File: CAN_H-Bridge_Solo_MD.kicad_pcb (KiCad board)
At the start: 2 copper layers, 84.9 x 45.3 mm, 45 parts, among them IC1 SI8650AB-B-IS1, IC2 A3921KLPTR-T, J2 Conn_01x03, J3 Conn_01x05, J4 Bus_mechaken_PCIexpress_x16_1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, M1 Motor_DC, Q1 IRLB3813PBF, Q2 IRLB3813PBF, Q3 IRLB3813PBF, Q4 IRLB3813PBF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

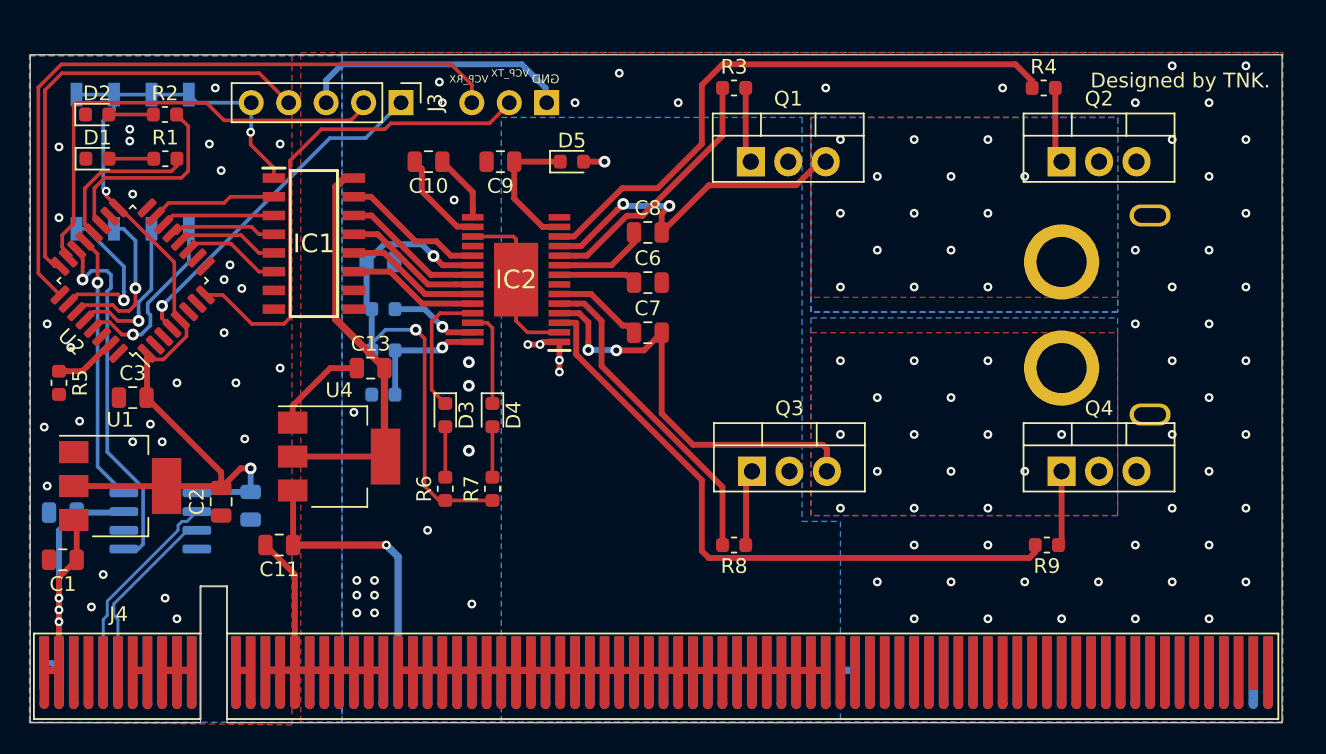
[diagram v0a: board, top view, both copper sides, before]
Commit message: change
FETのドレイン端子を移動
パッドを手はんだ用に変更
PCIeコネクタを変更
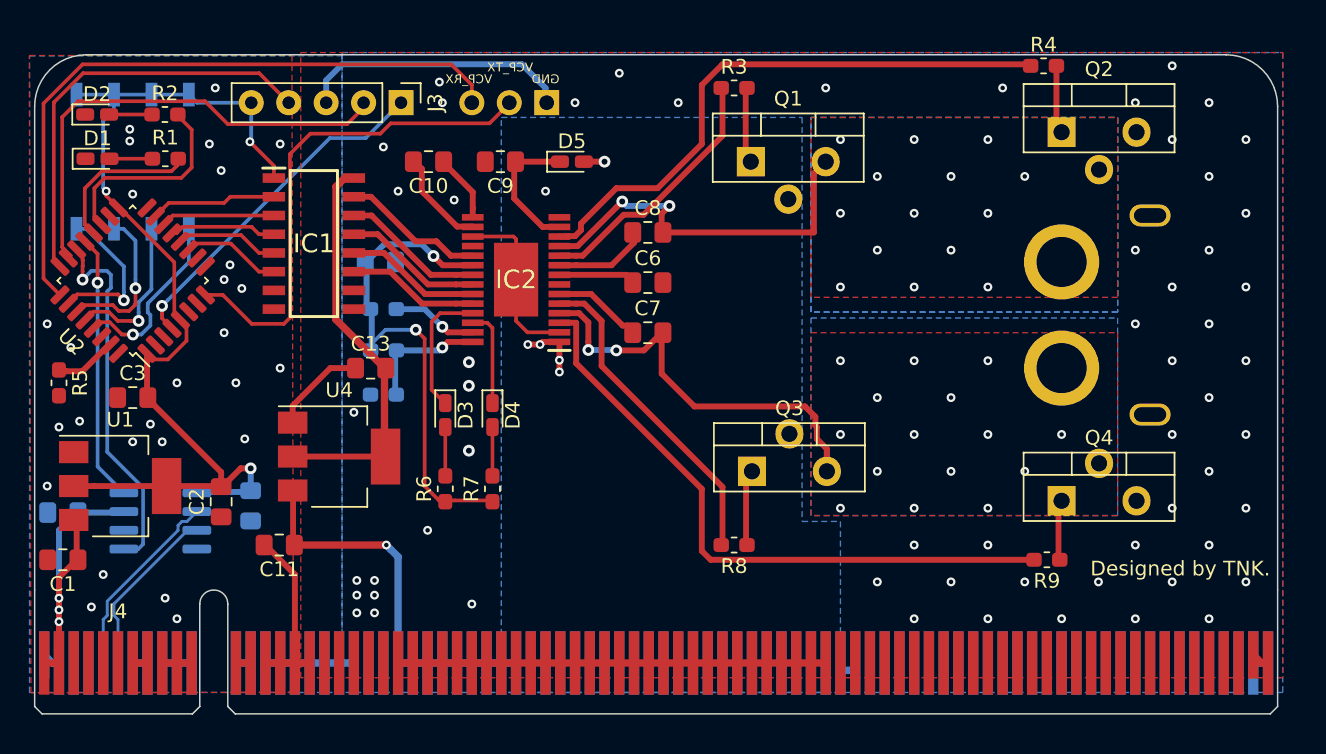
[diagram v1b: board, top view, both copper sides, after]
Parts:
- C1, C10, C11, C12, C13, C2, C3, C4, C5, C6, C7, C8, C9: footprint Capacitor_SMD:C_0805_2012Metric -> Capacitor_SMD:C_0805_2012Metric_Pad1.15x1.40mm_HandSolder
- D1, D2, D3, D4: footprint LED_SMD:LED_0603_1608Metric -> LED_SMD:LED_0603_1608Metric_Castellated
- D5: footprint Diode_SMD:D_0603_1608Metric -> LED_SMD:LED_0603_1608Metric_Castellated
- J4: footprint PCIe:BUS_mechaken_PCIexpress_x16_164_Position -> PCIe:BUS_mechaken_PCIexpress_x16
- R1, R10, R11, R12, R2, R3, R4, R5, R6, R7, R8, R9: footprint Resistor_SMD:R_0603_1608Metric -> Resistor_SMD:R_0603_1608Metric_Pad1.05x0.95mm_HandSolder
- moved Q2 2.00 mm to (145.0, 122.0)
- moved Q4 2.00 mm to (145.0, 147.0)
- moved R4 1.50 mm to (143.8, 117.5)
- moved R9 1.00 mm to (144.0, 151.0)
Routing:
- net GNDPWR: track 44.7 -> 39.9 mm, vias 57 -> 59
- net SA_0: track 23.8 -> 26.3 mm
- net /SWCLK: track 30.4 -> 28.9 mm
- net VCP_RX: track 46.5 -> 45.4 mm
- net Net-(Q4-Pad1): track 5.09 -> 4.09 mm
- net Net-(Q2-Pad1): track 5.18 -> 4.24 mm
- net SB_0: track 30.2 -> 29.4 mm
- net GLA_0: track 40.2 -> 39.4 mm
- net GLB_0: track 43.6 -> 43.0 mm
- net GND: vias 29 -> 27
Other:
- board size 84.9 x 45.3 mm -> 84.3 x 36.3 mm
- board text added: "CAN H-Bridge Solo MD Prototype 1.1"
- board text removed: "CAN H-Bridge Solo MD Prototype 1.0"

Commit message: change
レギュレータを新規に追加
その他細かな修正
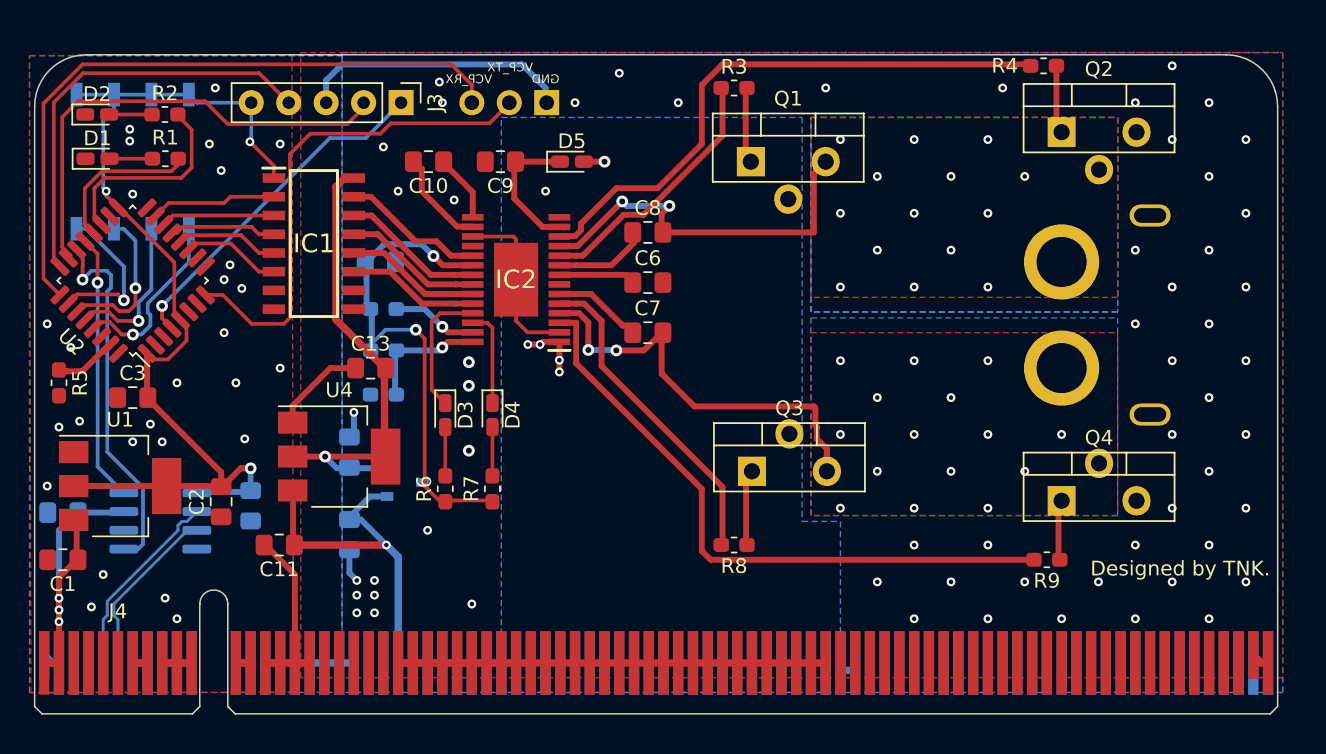
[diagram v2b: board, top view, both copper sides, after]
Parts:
- added C14: 2.2u, Capacitor_SMD:C_0805_2012Metric_Pad1.15x1.40mm_HandSolder, B.Cu at (96.7, 143.7)
- added C15: 1u, Capacitor_SMD:C_0805_2012Metric_Pad1.15x1.40mm_HandSolder, B.Cu at (96.7, 149.3)
- added IC3: AP7381-50SA-7, SamacSys_Parts:SOT96P240X105-3N, B.Cu at (100.5, 145.8)
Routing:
- net VCC: track 32.6 -> 39.2 mm
- net MD_3V3: track 27.5 -> 32.0 mm, vias 0 -> 1
- net GNDPWR: track 39.9 -> 44.0 mm

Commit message: clean
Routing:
- net GLB_0: track 43.0 -> 44.0 mm
- net V5: track 34.1 -> 34.7 mm
- net VCC: vias 6 -> 7
- net GNDPWR: vias 59 -> 61
- net GND: vias 27 -> 28
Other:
- board text added: "LED(ON:1 OFF:0) 00 -> Free 01 -> CW 10 -> CCW 11 -> Brake"
- board text added: "MSB"
- board text added: "Motor"

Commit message: clean
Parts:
- moved R8 10.0 mm to (122.6, 140.0)
- moved R3 7.00 mm to (122.8, 126.0)
- moved Q1 1.75 mm to (123.9, 122.2)
- moved Q3 1.75 mm to (124.0, 146.8)
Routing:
- net GHB_0: track 21.9 -> 15.2 mm
- net GHA_0: track 17.7 -> 12.7 mm
- net SB_0: track 29.8 -> 27.8 mm, vias 17 -> 16
- net Net-(Q3-Pad1): track 5.14 -> 6.96 mm
- net Net-(Q1-Pad1): track 5.14 -> 3.87 mm
- net GLB_0: track 44.0 -> 43.0 mm
- net VCC: track 39.2 -> 40.1 mm, vias 7 -> 8
- net SA_0: vias 16 -> 15

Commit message: release
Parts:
- Q1, Q2, Q3, Q4: value IRLB3813PBF -> IRFB3806PBF
- R1, R2, R6, R7: value 2.2K -> 2.2k
- R10: value 3K -> 3k
- R5: value 10K -> 10k
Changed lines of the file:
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@@
   )
   (setup
-    (last_trace_width 0.5)
+    (last_trace_width 0.25)
     (user_trace_width 0.4)
     (user_trace_width 0.5)
@@
     (tags "Integrated Circuit")
     (attr smd)
-    (fp_text reference IC3 (at 0 0 180) (layer B.SilkS)
+    (fp_text reference IC3 (at 0 0) (layer B.SilkS)
       (effects (font (size 1.27 1.27) (thickness 0.254)) (justify mirror))
     )
-    (fp_text value AP7381-50SA-7 (at 0 0 180) (layer B.SilkS) hide
+    (fp_text value AP7381-50SA-7 (at 0 0) (layer B.SilkS) hide
       (effects (font (size 1.27 1.27) (thickness 0.254)) (justify mirror))
     )
@@
     (fp_line (start 1.875 1.75) (end 1.875 -1.75) (layer B.CrtYd) (width 0.05))
     (fp_line (start -1.875 1.75) (end 1.875 1.75) (layer B.CrtYd) (width 0.05))
-    (fp_text user %R (at 0 0 180) (layer B.Fab)
+    (fp_text user %R (at 0 0) (layer B.Fab)
       (effects (font (size 1.27 1.27) (thickness 0.254)) (justify mirror))
     )
@@
       (effects (font (size 1 1) (thickness 0.15)) (justify mirror))
     )
-    (fp_text value 3K (at 0 -1.43) (layer B.Fab)
+    (fp_text value 3k (at 0 -1.43) (layer B.Fab)
       (effects (font (size 1 1) (thickness 0.15)) (justify mirror))
     )
@@
       (effects (font (size 1 1) (thickness 0.15)))
     )
-    (fp_text value 2.2K (at 0 1.43 90) (layer F.Fab)
+    (fp_text value 2.2k (at 0 1.43 90) (layer F.Fab)
       (effects (font (size 1 1) (thickness 0.15)))
     )
@@
       (effects (font (size 1 1) (thickness 0.15)))
     )
-    (fp_text value 2.2K (at 0 1.43 90) (layer F.Fab)
+    (fp_text value 2.2k (at 0 1.43 90) (layer F.Fab)
       (effects (font (size 1 1) (thickness 0.15)))
     )
@@
       (effects (font (size 1 1) (thickness 0.15)))
     )
-    (fp_text value 10K (at 0 1.43 90) (layer F.Fab)
+    (fp_text value 10k (at 0 1.43 90) (layer F.Fab)
       (effects (font (size 1 1) (thickness 0.15)))
     )
@@
       (effects (font (size 1 1) (thickness 0.15)))
     )
-    (fp_text value 2.2K (at 0 1.43) (layer F.Fab)
+    (fp_text value 2.2k (at 0 1.43) (layer F.Fab)
       (effects (font (size 1 1) (thickness 0.15)))
     )
@@
       (effects (font (size 1 1) (thickness 0.15)))
     )
-    (fp_text value 2.2K (at 0 1.43) (layer F.Fab)
+    (fp_text value 2.2k (at 0 1.43) (layer F.Fab)
       (effects (font (size 1 1) (thickness 0.15)))
     )
@@
       (effects (font (size 1 1) (thickness 0.15)))
     )
-    (fp_text value IRLB3813PBF (at 2.54 2.5) (layer F.Fab)
+    (fp_text value IRFB3806PBF (at 2.54 2.5) (layer F.Fab)
       (effects (font (size 1 1) (thickness 0.15)))
     )
@@
       (effects (font (size 1 1) (thickness 0.15)))
     )
-    (fp_text value IRLB3813PBF (at 2.54 2.5) (layer F.Fab)
+    (fp_text value IRFB3806PBF (at 2.54 2.5) (layer F.Fab)
       (effects (font (size 1 1) (thickness 0.15)))
     )
@@
       (effects (font (size 1 1) (thickness 0.15)))
     )
-    (fp_text value IRLB3813PBF (at 2.54 2.5) (layer F.Fab)
+    (fp_text value IRFB3806PBF (at 2.54 2.5) (layer F.Fab)
       (effects (font (size 1 1) (thickness 0.15)))
     )
@@
       (effects (font (size 1 1) (thickness 0.15)))
     )
-    (fp_text value IRLB3813PBF (at 2.58 2.5) (layer F.Fab)
-      (effects (font (size 1 1) (thickness 0.15)))
-    )
+    (fp_text value IRFB3806PBF (at 2.58 2.5) (layer F.Fab)
+      (effects (font (size 1 1) (thickness 0.15)))
+    )

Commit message: create
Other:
- board text added: "CAN H-Bridge Solo MD Prototype 1.2"
- board text removed: "CAN H-Bridge Solo MD Prototype 1.1"
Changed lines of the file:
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@@
   (gr_arc (start 78.85 120.25) (end 78.85 116.75) (angle -90) (layer Edge.Cuts) (width 0.1))
   (gr_arc (start 156.15 120.25) (end 159.65 120.25) (angle -90) (layer Edge.Cuts) (width 0.1))
-  (gr_text "CAN H-Bridge Solo MD\nPrototype 1.1" (at 135.6 120.8) (layer B.SilkS)
+  (gr_text "CAN H-Bridge Solo MD\nPrototype 1.2" (at 135.6 120.8) (layer B.SilkS)
     (effects (font (size 1 1) (thickness 0.15)) (justify mirror))
   )

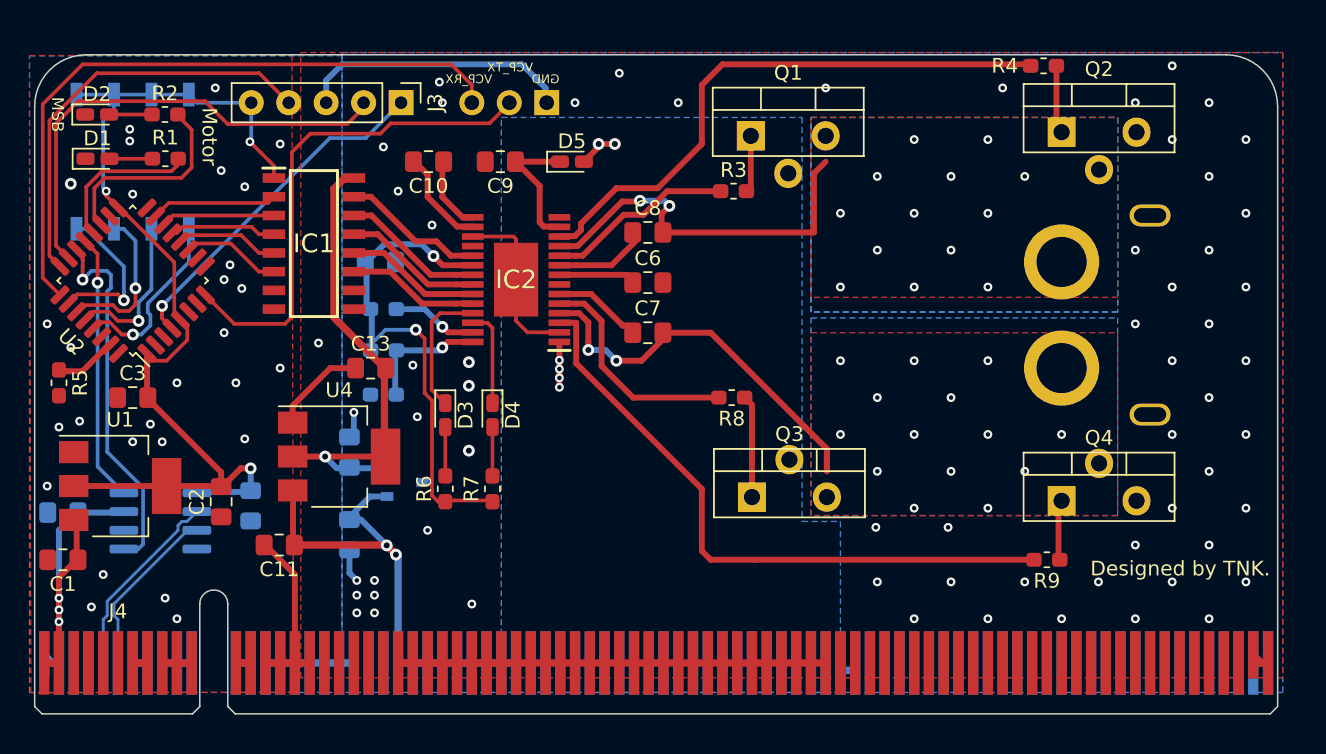
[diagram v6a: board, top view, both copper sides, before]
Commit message: clean
LEDの配線を変更
PA9 <-> PA10
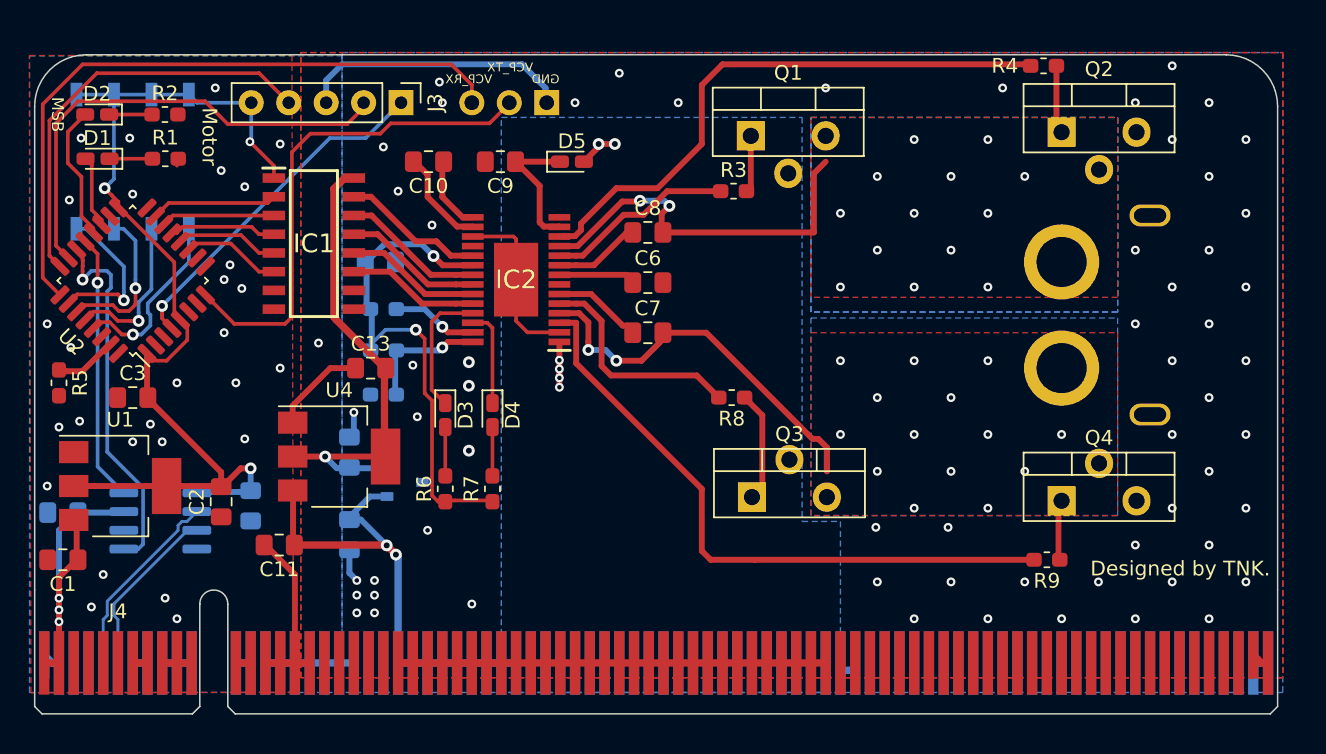
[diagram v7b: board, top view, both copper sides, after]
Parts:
- turned D1 to 180 degrees
- turned D2 to 180 degrees
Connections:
- D1 pad 1: GND -> Net-(D1-Pad1)
- D1 pad 2: Net-(D1-Pad2) -> MD0_LED_H
- D2 pad 1: GND -> Net-(D2-Pad1)
- D2 pad 2: Net-(D2-Pad2) -> MD0_LED_L
- R1 pad 1: Net-(D1-Pad2) -> Net-(D1-Pad1)
- R1 pad 2: MD0_LED_H -> GND
- R2 pad 1: Net-(D2-Pad2) -> Net-(D2-Pad1)
- R2 pad 2: MD0_LED_L -> GND
- U2 pad 19: MD0_LED_L -> MD0_LED_H
- U2 pad 20: MD0_LED_H -> MD0_LED_L
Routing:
- net MD0_LED_H: track 10.5 -> 5.62 mm
- net MD0_LED_L: track 13.9 -> 9.92 mm
- net Net-(D2-Pad2): track 3.03 -> 0.00 mm
- net Net-(D2-Pad1): track 0.00 -> 3.03 mm
- net Net-(D1-Pad2): track 3.02 -> 0.00 mm
- net Net-(D1-Pad1): track 0.00 -> 3.02 mm
- net Net-(Q3-Pad1): track 6.96 -> 7.54 mm
- added copper zone on F.Cu, net VCC

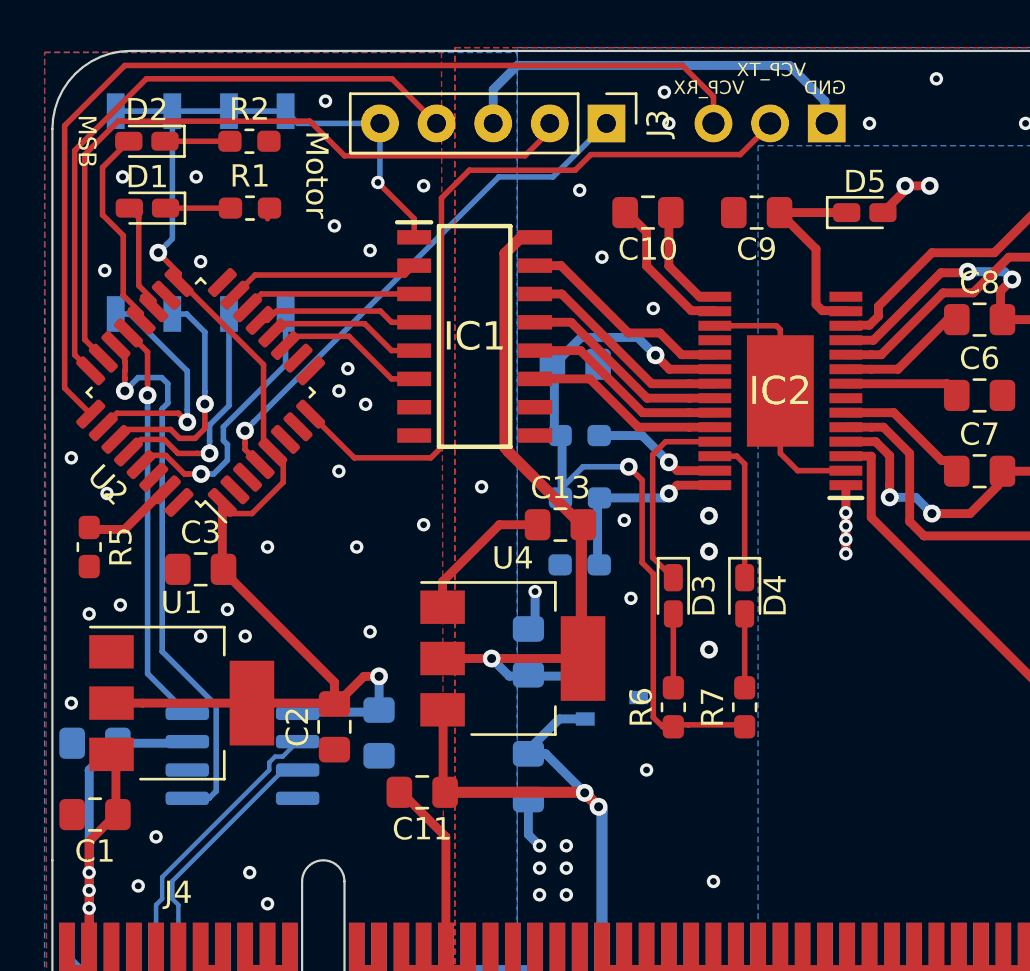
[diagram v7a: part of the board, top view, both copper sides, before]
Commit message: add
LDOの逆電圧防止用にSBDを追加
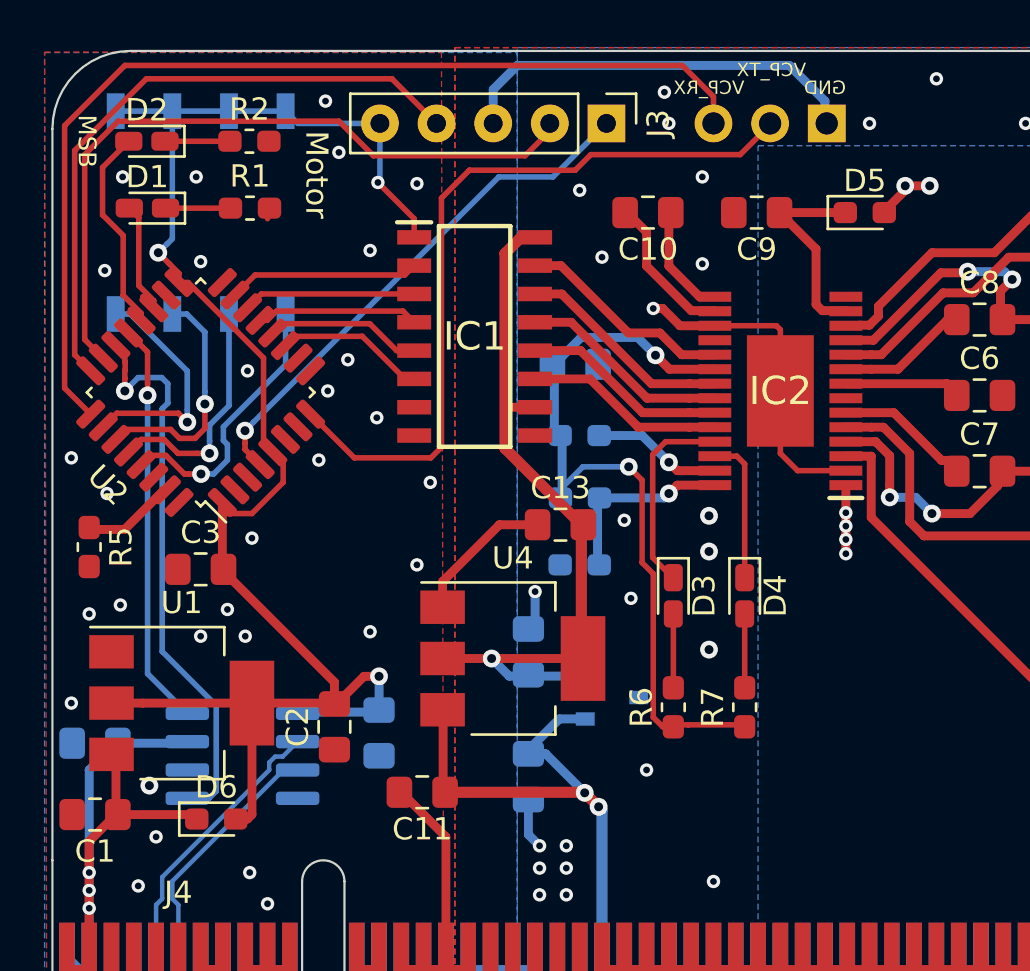
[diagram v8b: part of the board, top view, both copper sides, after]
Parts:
- added D6: D_Schottky, Diode_SMD:D_0603_1608Metric_Pad1.05x0.95mm_HandSolder, F.Cu at (82.7, 151.2)
- D5: footprint LED_SMD:LED_0603_1608Metric_Castellated -> Diode_SMD:D_0603_1608Metric_Pad1.05x0.95mm_HandSolder
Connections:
- IC1 pad 10: Net-(IC1-Pad10) -> MD_3V3
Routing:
- net +3V3: track 69.7 -> 75.6 mm
- net +5V: track 28.1 -> 31.8 mm
- net GNDPWR: track 44.0 -> 47.1 mm, vias 61 -> 62
- net MD_3V3: track 32.1 -> 33.5 mm
- net GND: vias 28 -> 30
